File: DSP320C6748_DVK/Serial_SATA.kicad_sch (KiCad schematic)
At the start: 42 parts, among them IC10 CP2102C-A01-GQFN24, IC9 CDCM61001RHBT, J5 SAT3M3232012TR, J6 USB_Type_C, Y3 25MHz

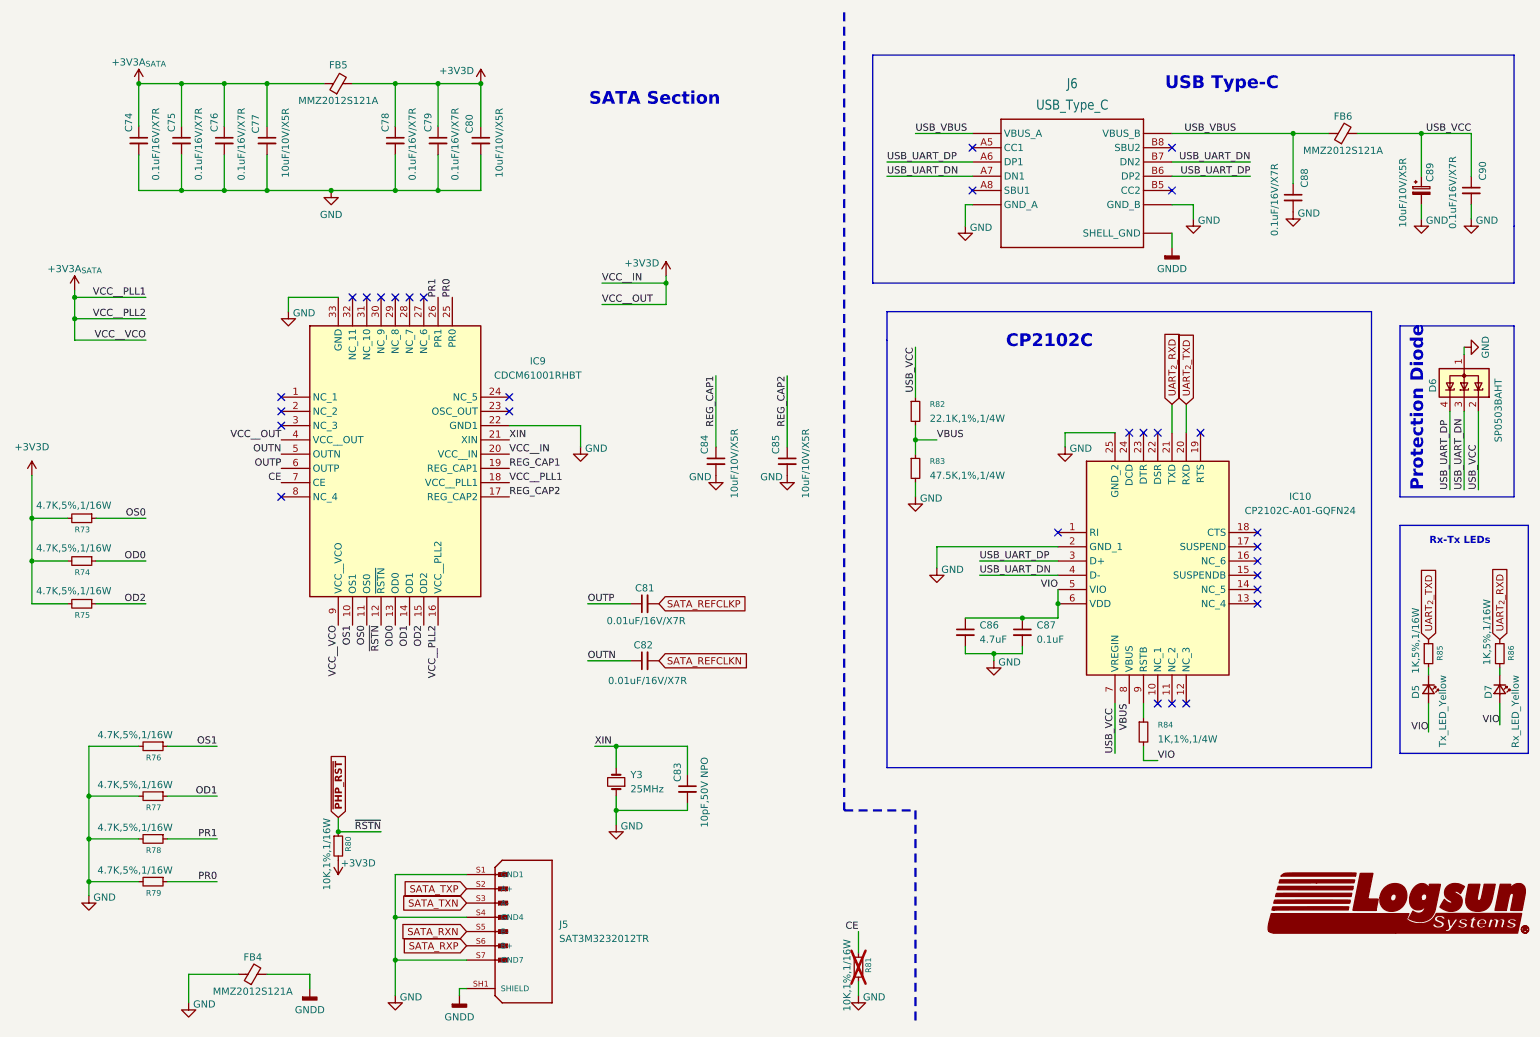
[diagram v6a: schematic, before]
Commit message: Scheamtic Re-annotation done, Some footprints assigned
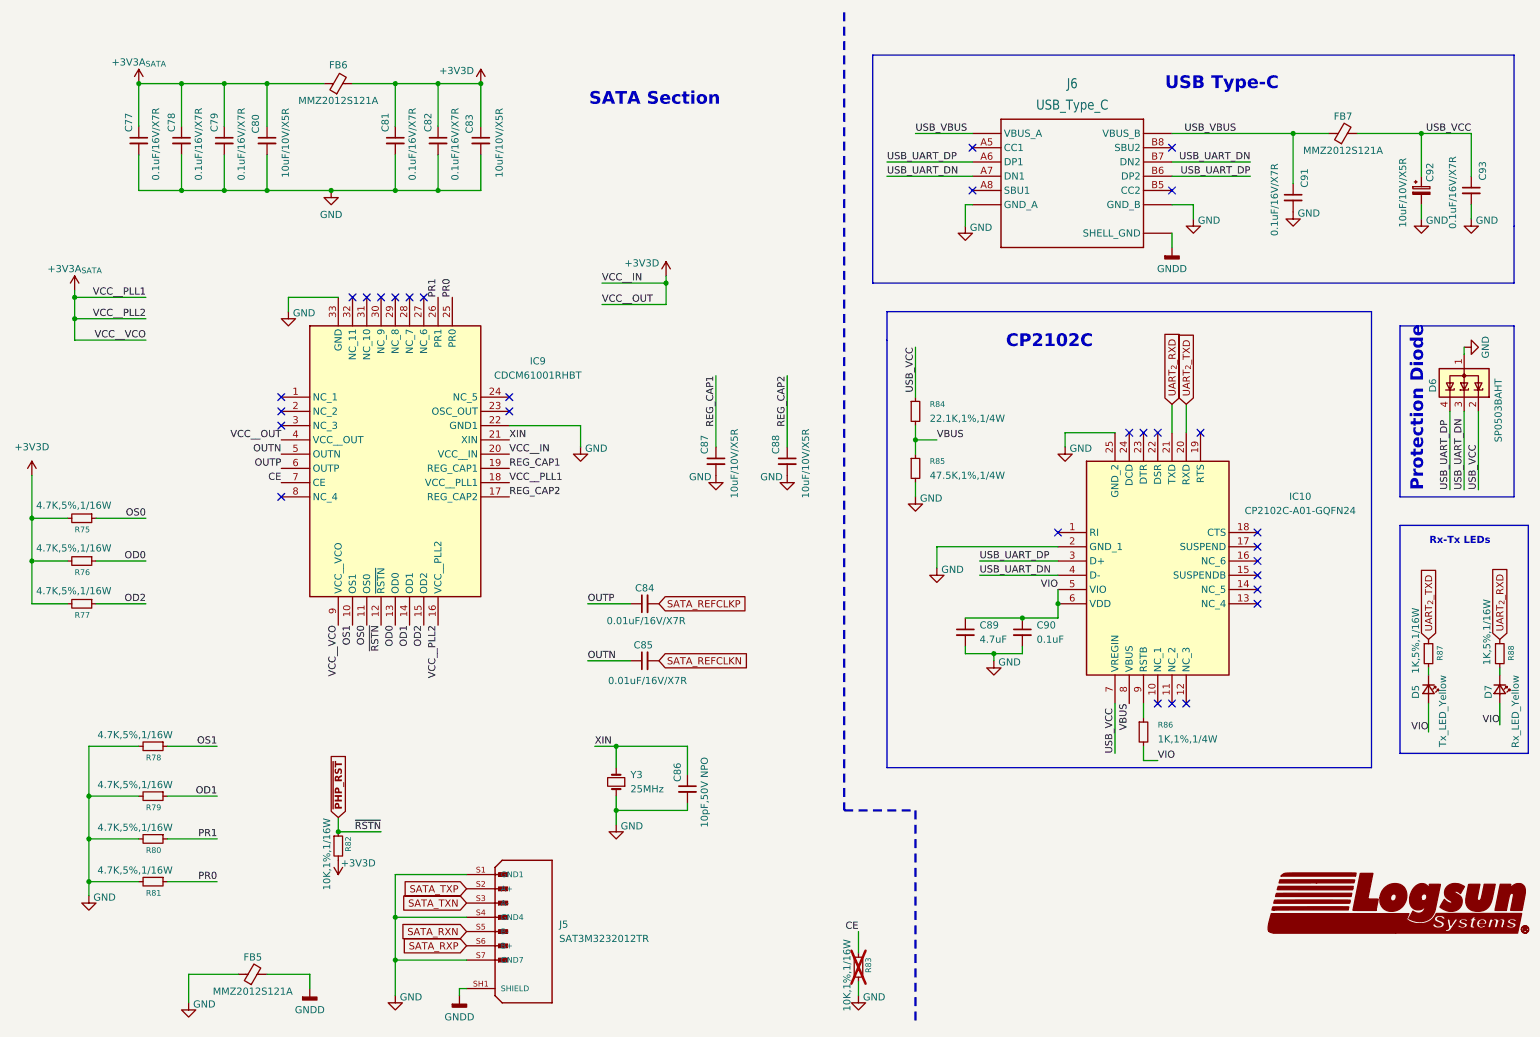
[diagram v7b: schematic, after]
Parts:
- C77: renamed from C74; footprint (none) -> Capacitor_SMD:C_0603_1608Metric_Pad1.08x0.95mm_HandSolder
- C78: renamed from C75; footprint (none) -> Capacitor_SMD:C_0603_1608Metric_Pad1.08x0.95mm_HandSolder
- C79: renamed from C76; footprint (none) -> Capacitor_SMD:C_0603_1608Metric_Pad1.08x0.95mm_HandSolder
- C80: renamed from C77; footprint (none) -> Capacitor_SMD:C_0603_1608Metric_Pad1.08x0.95mm_HandSolder
- C81: renamed from C78; footprint (none) -> Capacitor_SMD:C_0603_1608Metric_Pad1.08x0.95mm_HandSolder
- C82: renamed from C79; footprint (none) -> Capacitor_SMD:C_0603_1608Metric_Pad1.08x0.95mm_HandSolder
- C83: renamed from C80; footprint (none) -> Capacitor_SMD:C_0603_1608Metric_Pad1.08x0.95mm_HandSolder
- C84: renamed from C81; footprint (none) -> Capacitor_SMD:C_0603_1608Metric_Pad1.08x0.95mm_HandSolder
- C85: renamed from C82; footprint (none) -> Capacitor_SMD:C_0603_1608Metric_Pad1.08x0.95mm_HandSolder
- C86: renamed from C83; footprint (none) -> Capacitor_SMD:C_0603_1608Metric_Pad1.08x0.95mm_HandSolder
- C87: renamed from C84; footprint (none) -> Capacitor_SMD:C_0603_1608Metric_Pad1.08x0.95mm_HandSolder
- C88: renamed from C85; footprint (none) -> Capacitor_SMD:C_0603_1608Metric_Pad1.08x0.95mm_HandSolder
- C89: renamed from C86; footprint (none) -> Capacitor_SMD:C_0603_1608Metric_Pad1.08x0.95mm_HandSolder
- C90: renamed from C87; footprint (none) -> Capacitor_SMD:C_0603_1608Metric_Pad1.08x0.95mm_HandSolder
- C91: renamed from C88; footprint (none) -> Capacitor_SMD:C_0603_1608Metric_Pad1.08x0.95mm_HandSolder
- C92: renamed from C89; footprint (none) -> Capacitor_SMD:C_0603_1608Metric_Pad1.08x0.95mm_HandSolder
- C93: renamed from C90; footprint (none) -> Capacitor_SMD:C_0603_1608Metric_Pad1.08x0.95mm_HandSolder
- FB5: renamed from FB4; footprint (none) -> Inductor_SMD:L_0805_2012Metric_Pad1.05x1.20mm_HandSolder
- FB6: renamed from FB5; footprint (none) -> Inductor_SMD:L_0805_2012Metric_Pad1.05x1.20mm_HandSolder
- FB7: renamed from FB6; footprint (none) -> Inductor_SMD:L_0805_2012Metric_Pad1.05x1.20mm_HandSolder
- IC9: footprint QFN50P500X500X100-33N-D -> TPS650250RHBR:QFN50P500X500X100-33N-D
- R75: renamed from R73; footprint (none) -> Resistor_SMD:R_0603_1608Metric_Pad0.98x0.95mm_HandSolder
- R76: renamed from R74; footprint (none) -> Resistor_SMD:R_0603_1608Metric_Pad0.98x0.95mm_HandSolder
- R77: renamed from R75; footprint (none) -> Resistor_SMD:R_0603_1608Metric_Pad0.98x0.95mm_HandSolder
- R78: renamed from R76; footprint (none) -> Resistor_SMD:R_0603_1608Metric_Pad0.98x0.95mm_HandSolder
- R79: renamed from R77; footprint (none) -> Resistor_SMD:R_0603_1608Metric_Pad0.98x0.95mm_HandSolder
- R80: renamed from R78; footprint (none) -> Resistor_SMD:R_0603_1608Metric_Pad0.98x0.95mm_HandSolder
- R81: renamed from R79; footprint (none) -> Resistor_SMD:R_0603_1608Metric_Pad0.98x0.95mm_HandSolder
- R82: renamed from R80; footprint (none) -> Resistor_SMD:R_0603_1608Metric_Pad0.98x0.95mm_HandSolder
- R83: renamed from R81; footprint (none) -> Resistor_SMD:R_0603_1608Metric_Pad0.98x0.95mm_HandSolder
- R84: renamed from R82; footprint (none) -> Resistor_SMD:R_0603_1608Metric_Pad0.98x0.95mm_HandSolder
- R85: renamed from R83; footprint (none) -> Resistor_SMD:R_0603_1608Metric_Pad0.98x0.95mm_HandSolder
- R86: renamed from R84; footprint (none) -> Resistor_SMD:R_0603_1608Metric_Pad0.98x0.95mm_HandSolder
- R87: renamed from R85; footprint (none) -> Resistor_SMD:R_0603_1608Metric_Pad0.98x0.95mm_HandSolder
- R88: renamed from R86; footprint (none) -> Resistor_SMD:R_0603_1608Metric_Pad0.98x0.95mm_HandSolder
